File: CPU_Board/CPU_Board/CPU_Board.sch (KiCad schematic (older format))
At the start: 110 parts, among them J101 Screw_Terminal_01x03, J102 Conn_02x01, J103 Conn_02x01, J104 Conn_01x08_Male, J105 Conn_02x09_Odd_Even, J106 Micro_SD_Card_Det, J107 Conn_01x06_Male, J108 Conn_02x01, J109 Conn_02x01, J110 Screw_Terminal_01x04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

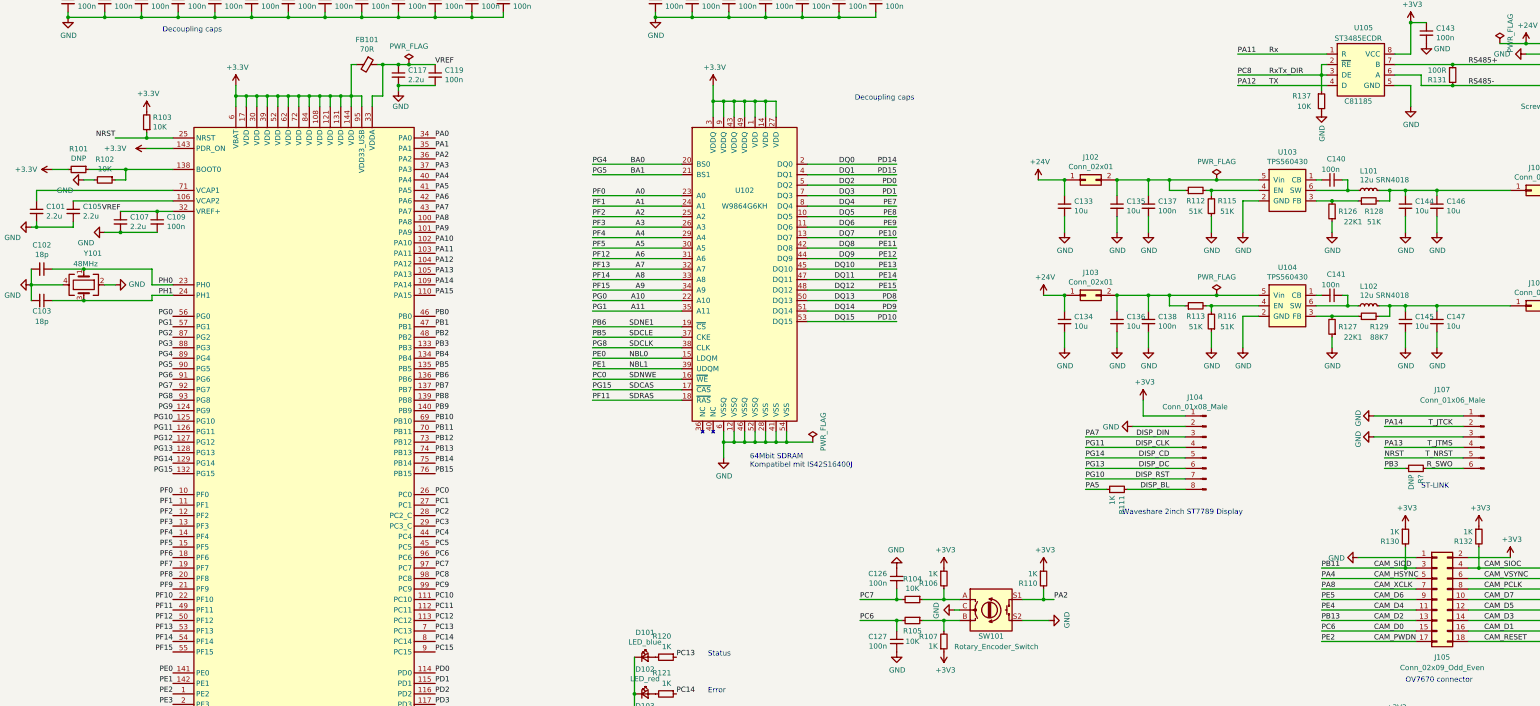
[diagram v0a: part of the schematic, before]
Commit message: PCB fertig. Length matching RAM 55mm, DCMI 90mm, SD-Card 65mm.. Pins für interfaces erneut mit Evalboard und CubeMX muxtool verglichen
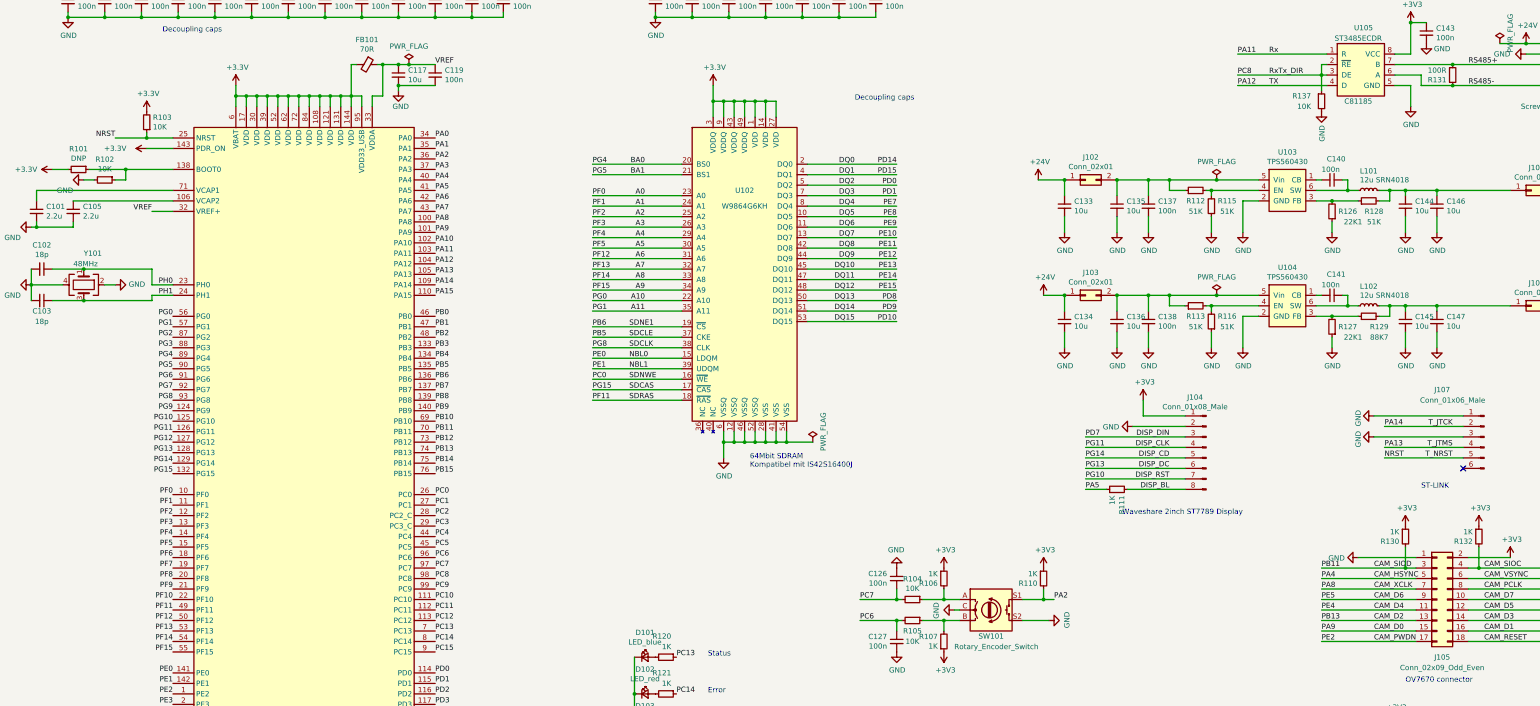
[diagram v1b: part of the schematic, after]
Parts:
- removed C107: 2.2u, Capacitor_SMD:C_1210_3225Metric, symbol Device:C_Small
- removed C109: 100n, Capacitor_SMD:C_0603_1608Metric, symbol Device:C_Small
- removed R?: DNP, Resistor_SMD:R_0603_1608Metric, symbol Device:R_Small
- C117: value 2.2u -> 10u
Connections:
- net PA9 is gone; now on net CAM_D0: U101.101 (PA9)
- net PD7 is gone; now on net DISP_DIN: U101.123 (PD7)
- net CAM_D0: no longer C127.1, R105.2, U101.96 (PC6)
- net DISP_DIN: no longer R109.1, U101.43 (PA7)
- net R_SWO: no longer names the net of J107.6 (Pin_6)
- new net PA7: R109.1, U101.43 (PA7)
- new net PC6: C127.1, R105.2, U101.96 (PC6)
- no-connect marks 1 -> 2
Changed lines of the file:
@@
 VREF
 Connection ~ 4250 1600
-Text Label 1750 3000 2    50   ~ 0
+Text Label 2050 3000 2    50   ~ 0
 VREF
-Wire Wire Line
-	1750 3000 2100 3000
-$Comp
-L Device:C_Small C?
-U 1 1 60053E11
-P 1750 3100
-AR Path="/5FDD0F66/60053E11" Ref="C?"  Part="1"
-AR Path="/60053E11" Ref="C107"  Part="1"
-F 0 "C107" H 1842 3146 50  0000 L CNN
-F 1 "2.2u" H 1842 3055 50  0000 L CNN
-F 2 "Capacitor_SMD:C_1210_3225Metric" H 1750 3100 50  0001 C CNN
-F 3 "~" H 1750 3100 50  0001 C CNN
-F 4 " C696854 " H 1750 3100 50  0001 C CNN "LCSC"
-	1    1750 3100
-	1    0    0    -1
-$EndComp
 $Comp
 L Device:C_Small C?
@@
 AR Path="/60053E19" Ref="C117"  Part="1"
 F 0 "C117" H 4492 1746 50  0000 L CNN
-F 1 "2.2u" H 4492 1655 50  0000 L CNN
+F 1 "10u" H 4492 1655 50  0000 L CNN
 F 2 "Capacitor_SMD:C_1210_3225Metric" H 4400 1700 50  0001 C CNN
 F 3 "~" H 4400 1700 50  0001 C CNN
@@
 	1    0    0    -1
 $EndComp
-$Comp
-L Device:C_Small C?
-U 1 1 60053E2B
-P 2100 3100
-AR Path="/5FDD0F66/60053E2B" Ref="C?"  Part="1"
-AR Path="/60053E2B" Ref="C109"  Part="1"
-F 0 "C109" H 2192 3146 50  0000 L CNN
-F 1 "100n" H 2192 3055 50  0000 L CNN
-F 2 "Capacitor_SMD:C_0603_1608Metric" H 2100 3100 50  0001 C CNN
-F 3 "~" H 2100 3100 50  0001 C CNN
-F 4 "C83060" H 2100 3100 50  0001 C CNN "LCSC"
-	1    2100 3100
-	1    0    0    -1
-$EndComp
-Connection ~ 2100 3000
-Wire Wire Line
-	2100 3000 2250 3000
-Wire Wire Line
-	2100 3200 1750 3200
-$Comp
-L power:GND #PWR?
-U 1 1 60053E35
-P 1600 3200
-AR Path="/5FDD0F66/60053E35" Ref="#PWR?"  Part="1"
-AR Path="/60053E35" Ref="#PWR0107"  Part="1"
-F 0 "#PWR0107" H 1600 2950 50  0001 C CNN
-F 1 "GND" V 1700 3100 50  0000 R CNN
-F 2 "" H 1600 3200 50  0001 C CNN
-F 3 "" H 1600 3200 50  0001 C CNN
-	1    1600 3200
-	0    1    1    0
-$EndComp
-Wire Wire Line
-	1750 3200 1600 3200
-Connection ~ 1750 3200
 $Comp
 L power:GND #PWR?
@@
 Text Label 14450 5350 2    50   ~ 0
 T_NRST
-Text Label 14450 5450 2    50   ~ 0
-R_SWO
 Wire Wire Line
 	14550 5150 13700 5150
@@
 Wire Wire Line
 	13800 5350 14550 5350
-Wire Wire Line
-	14200 5450 14550 5450
 Text Label 13800 5250 0    50   ~ 0
 PA13
@@
 Wire Wire Line
 	13800 5050 14550 5050
-Text Label 13800 5450 0    50   ~ 0
-PB3
 Text Notes 14150 5650 0    50   ~ 0
 ST-LINK
@@
 PG9
 Text Label 13200 7000 0    50   ~ 0
-PC6
+PA9
 Text Label 15400 7000 0    50   ~ 0
 PA10
@@
 Wire Wire Line
 	10600 6900 10350 6900
-Text Label 8800 6900 0    50   ~ 0
-PC6
 Text Label 8800 6700 0    50   ~ 0
 PC7
@@
 PG11
 Text Label 10950 5150 0    50   ~ 0
-PA7
+PD7
 Wire Wire Line
 	10950 5150 11900 5150
@@
 Text Notes 7350 7600 0    50   ~ 0
 Error
-$Comp
-L Device:R_Small R?
-U 1 1 600784DB
-P 14100 5450
-AR Path="/5FDD0F66/600784DB" Ref="R?"  Part="1"
-AR Path="/600784DB" Ref="R?"  Part="1"
-F 0 "R?" H 14041 5404 50  0000 R CNN
-F 1 "DNP" H 14041 5495 50  0000 R CNN
-F 2 "Resistor_SMD:R_0603_1608Metric" H 14100 5450 50  0001 C CNN
-F 3 "~" H 14100 5450 50  0001 C CNN
-F 4 "C14676" H 14100 5450 50  0001 C CNN "LCSC"
-	1    14100 5450
-	0    -1   -1   0
-$EndComp
-Wire Wire Line
-	14000 5450 13800 5450
+Wire Wire Line
+	2050 3000 2250 3000
+Text Label 8800 6900 0    50   ~ 0
+PC6
+NoConn ~ 14550 5450
 $EndSCHEMATC
